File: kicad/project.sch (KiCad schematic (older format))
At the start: 0 parts

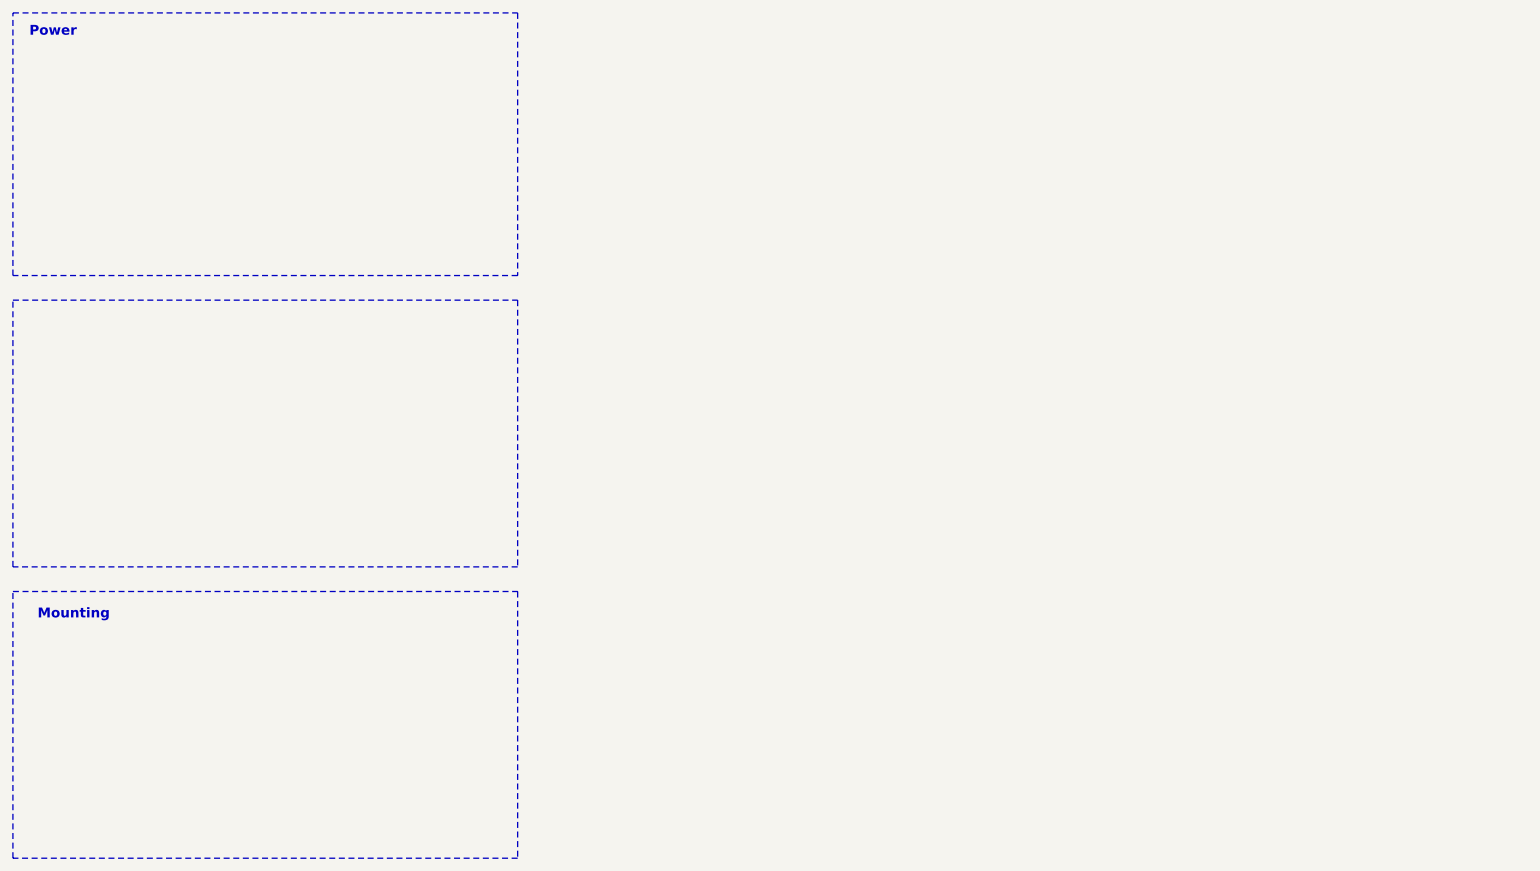
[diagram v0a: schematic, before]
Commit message: APA102C for the leds
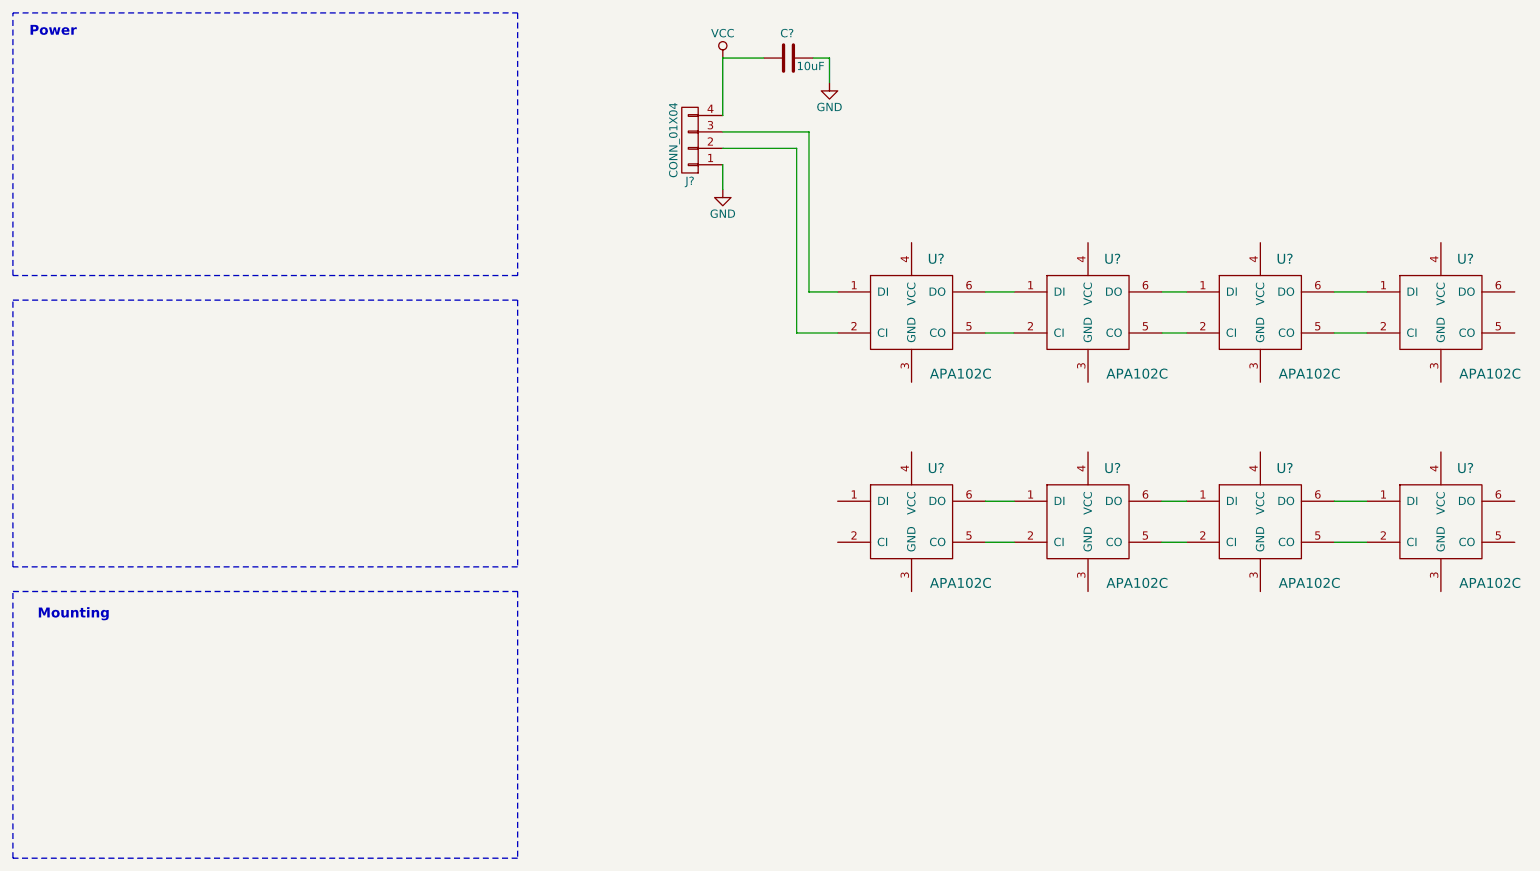
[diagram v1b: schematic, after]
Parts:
- added C?: 10uF, symbol C
- added J?: CONN_01X04, symbol CONN_01X04
- added U? (x8): APA102C, symbol APA102C
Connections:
- new net: J?.3 (P3), U?.1 (DI)
- new net: J?.2 (P2), U?.2 (CI)
- new net: U?.2 (CI), U?.5 (CO) (x6)
- new net: U?.1 (DI), U?.6 (DO) (x6)
- new net GND: C?.1, J?.1 (P1)
- new net VCC: C?.2, J?.4 (P4)

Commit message: 4 leds only
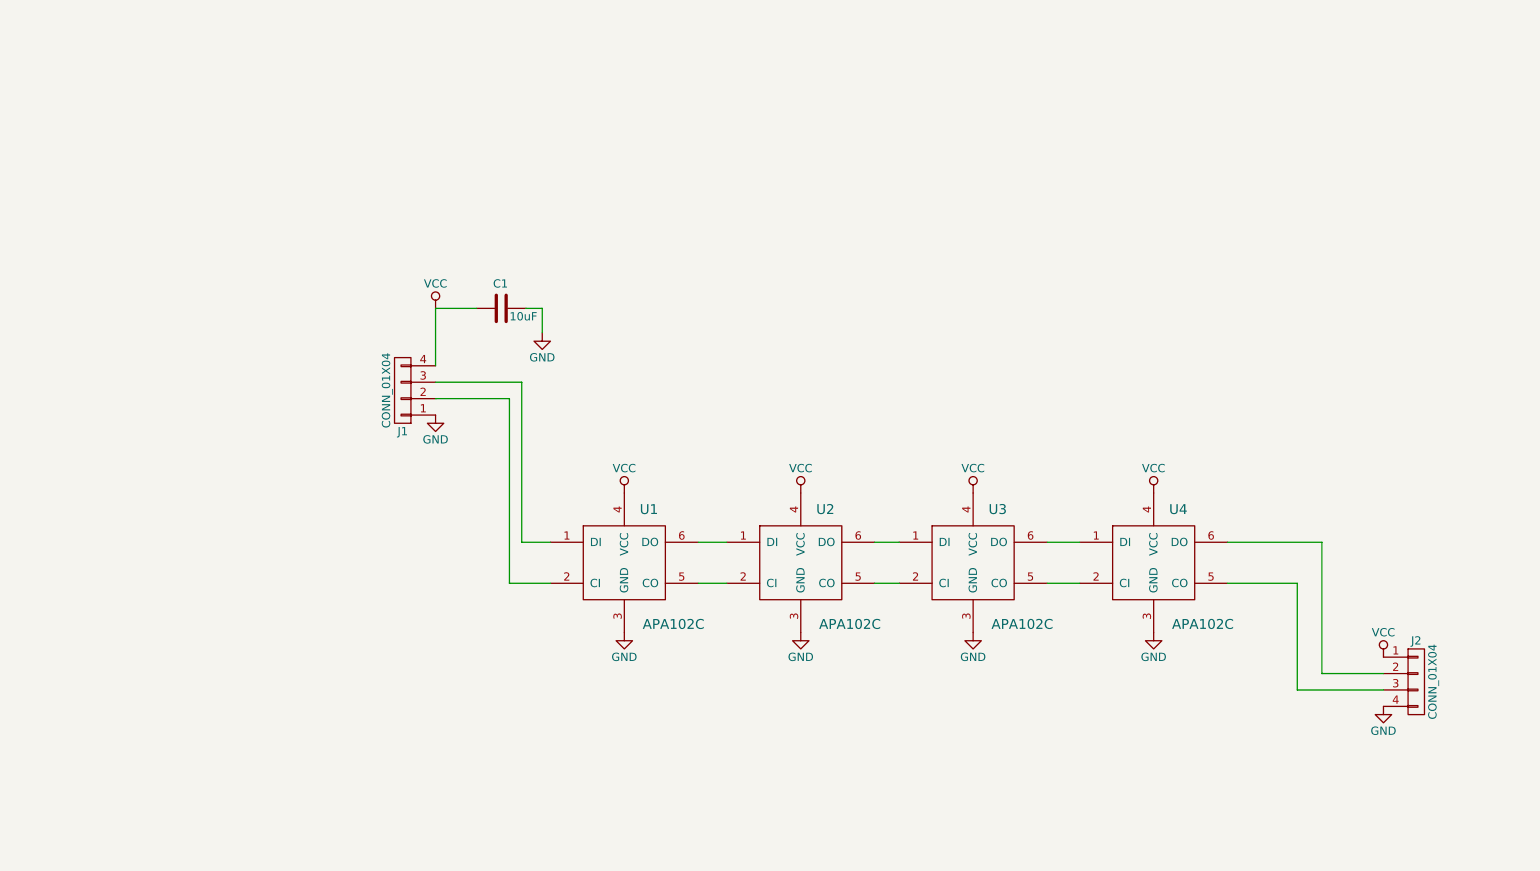
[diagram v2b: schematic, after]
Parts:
- removed U? (x4): APA102C, symbol APA102C
- added J2: CONN_01X04, Pin_Headers:Pin_Header_Straight_1x04_Pitch2.54mm, symbol CONN_01X04
- C1: renamed from C?; footprint (none) -> Capacitors_SMD:C_0805_HandSoldering
- J1: renamed from J?; footprint (none) -> Pin_Headers:Pin_Header_Straight_1x04_Pitch2.54mm
- U1, U2, U3, U4: renamed from U?; footprint (none) -> LEDs:LED_WS2812-PLCC6
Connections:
- net GND: now also U1.3 (GND), U2.3 (GND), U3.3 (GND), U4.3 (GND), J2.4 (P4)
- net VCC: now also U1.4 (VCC), U2.4 (VCC), U3.4 (VCC), U4.4 (VCC), J2.1 (P1)
- net at U4.5 (CO): now also J2.3 (P3)
- net at U4.6 (DO): now also J2.2 (P2)
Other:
- note removed: "Mounting"
- note removed: "Power"
- moved on the sheet: C1, J1, U1, U2, U3, U4
